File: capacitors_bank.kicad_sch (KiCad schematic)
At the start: 41 parts, among them K401 HF3F-L-12-1ZL2T, K402 HF3F-L-12-1ZL2T, K403 HF3F-L-12-1ZL2T, K404 HF3F-L-12-1ZL2T, K405 HF3F-L-12-1ZL2T, K406 HF3F-L-12-1ZL2T, K407 HF3F-L-12-1ZL2T, K408 HF3F-L-12-1ZL2T, Q401 PMOS, Q402 PMOS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

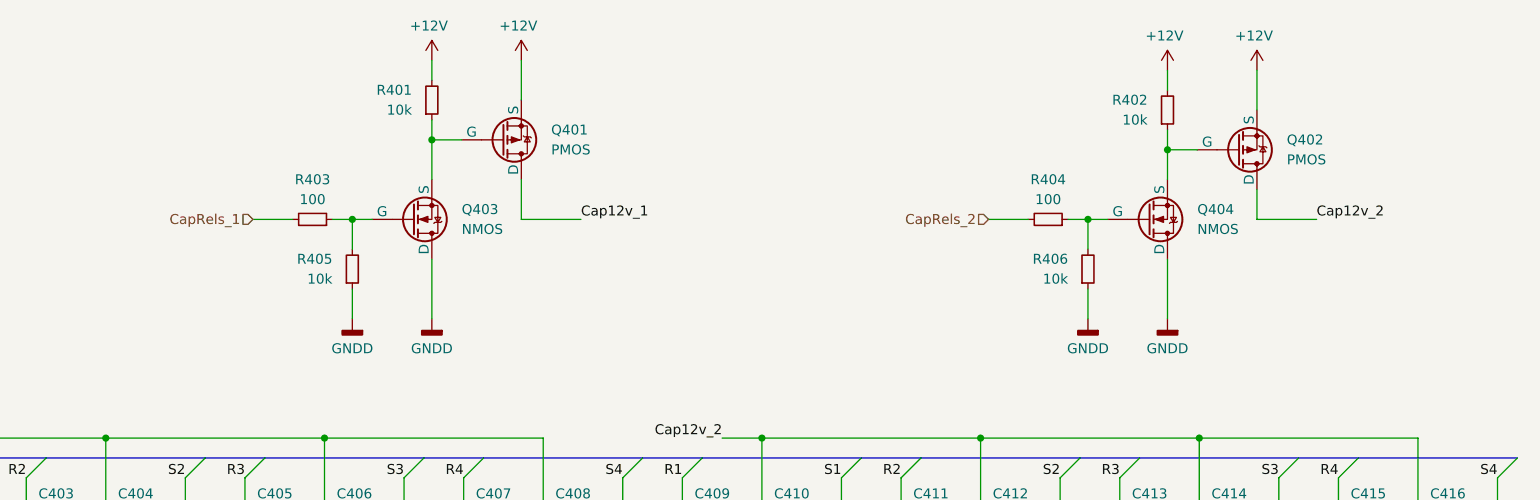
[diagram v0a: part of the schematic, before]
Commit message: Many more vias, improved some routing
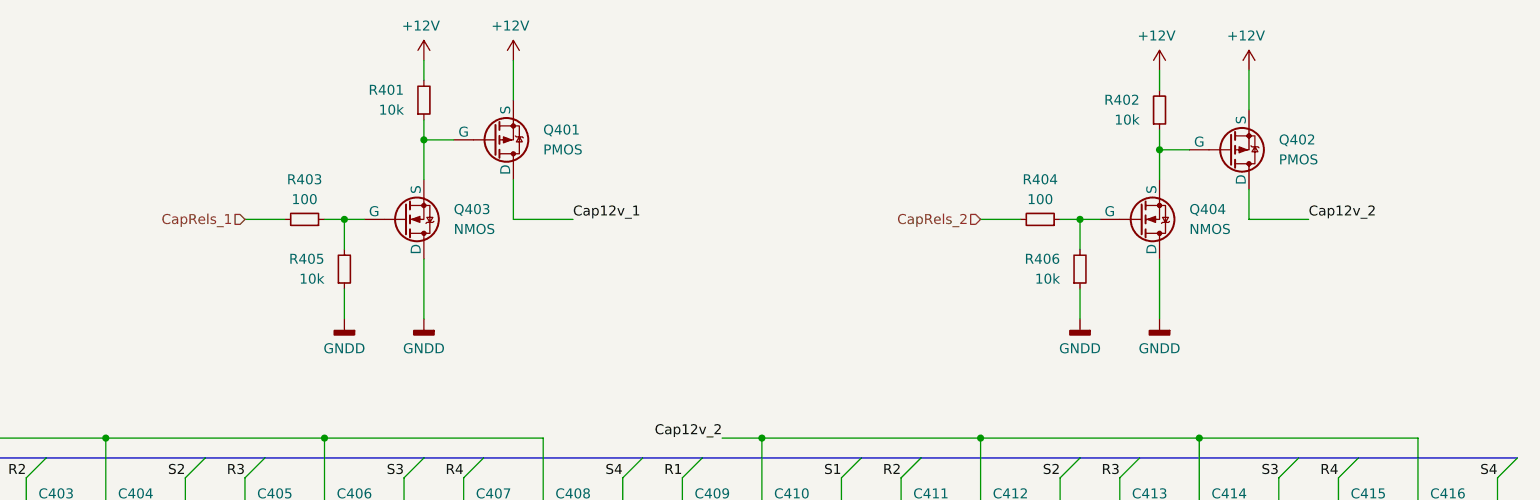
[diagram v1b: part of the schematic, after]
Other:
- moved on the sheet: Q401, Q402, Q403, Q404, R401, R402, R403, R404, R405, R406

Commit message: Some schematic cleanup and minor fixes
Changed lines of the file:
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@@
 	(title_block
 		(title "Capacitors Bank")
-		(date "2024-04-23")
+		(date "2024-04-26")
 		(rev "A0")
 		(company "TiZed")
@@
 	(bus
 		(pts
-			(xy 68.58 86.36) (xy 68.58 106.68)
+			(xy 68.58 99.06) (xy 68.58 106.68)
 		)
 		(stroke
@@
 	(bus
 		(pts
-			(xy 62.23 86.36) (xy 68.58 86.36)
+			(xy 62.23 99.06) (xy 68.58 99.06)
 		)
 		(stroke
@@
 	(hierarchical_label "{S[1..4] R[1..4]}"
 		(shape input)
-		(at 62.23 86.36 180)
-		(fields_autoplaced yes)
-		(effects
+		(at 62.23 99.06 180)
+		(fields_autoplaced yes)
+		(effects

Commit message: Added transistors parts. Added reverse polarity protection, pending adding to layout
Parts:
- Q401, Q402: value PMOS -> AO3401A
- Q403, Q404: value NMOS -> AO3400
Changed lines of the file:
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@@
 			)
 		)
-		(property "Value" "NMOS"
+		(property "Value" "AO3400"
 			(at 133.35 77.4699 0)
 			(effects
@@
 			)
 		)
-		(property "Datasheet" "https://ngspice.sourceforge.io/docs/ngspice-html-manual/manual.xhtml#cha_MOSFETs"
+		(property "Datasheet" "~"
 			(at 127 63.5 0)
 			(effects
@@
 			)
 		)
-		(property "Value" "NMOS"
+		(property "Value" "AO3400"
 			(at 227.33 77.4699 0)
 			(effects
@@
 			)
 		)
-		(property "Datasheet" "https://ngspice.sourceforge.io/docs/ngspice-html-manual/manual.xhtml#cha_MOSFETs"
+		(property "Datasheet" "~"
 			(at 220.98 63.5 0)
 			(effects
@@
 			)
 		)
-		(property "Value" "PMOS"
+		(property "Value" "AO3401A"
 			(at 238.76 68.5799 0)
 			(effects
@@
 			)
 		)
-		(property "Datasheet" "https://ngspice.sourceforge.io/docs/ngspice-html-manual/manual.xhtml#cha_MOSFETs"
+		(property "Datasheet" "~"
 			(at 232.41 54.61 0)
 			(effects
@@
 			)
 		)
-		(property "Value" "PMOS"
+		(property "Value" "AO3401A"
 			(at 144.78 67.3099 0)
 			(effects
@@
 			)
 		)
-		(property "Datasheet" "https://ngspice.sourceforge.io/docs/ngspice-html-manual/manual.xhtml#cha_MOSFETs"
+		(property "Datasheet" "~"
 			(at 138.43 53.34 0)
 			(effects
